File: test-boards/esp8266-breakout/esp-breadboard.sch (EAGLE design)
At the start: 6 parts

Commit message: cleanup to esp breadboard breakout
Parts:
- JP1: device esp:I2C_STANDARD -> esp:I2C_STANDARD_NO_SILK
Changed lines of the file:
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@@
 <part name="C1" library="rcl" deviceset="C-EU" device="C0805" value="1u"/>
 <part name="SUPPLY2" library="supply2" deviceset="GND" device=""/>
-<part name="JP1" library="esp" deviceset="I2C_STANDARD" device="" value="0"/>
+<part name="JP1" library="esp" deviceset="I2C_STANDARD" device="_NO_SILK" value="0"/>
 <part name="FRAME1" library="frames" deviceset="A4L-LOC" device="" value="ESP"/>
 <part name="SUPPLY3" library="supply2" deviceset="GND" device=""/>

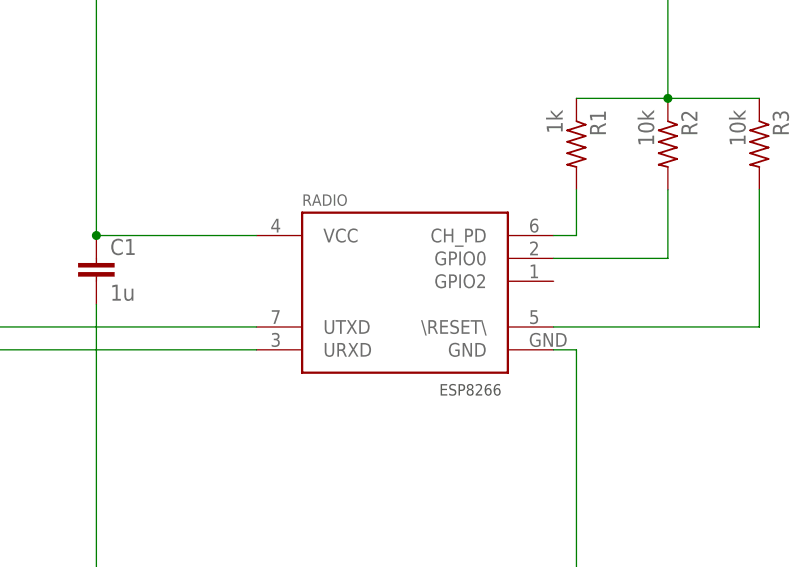
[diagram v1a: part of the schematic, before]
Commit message: ESP8266: misplaced RX and GPIO pin, switch around and resize board
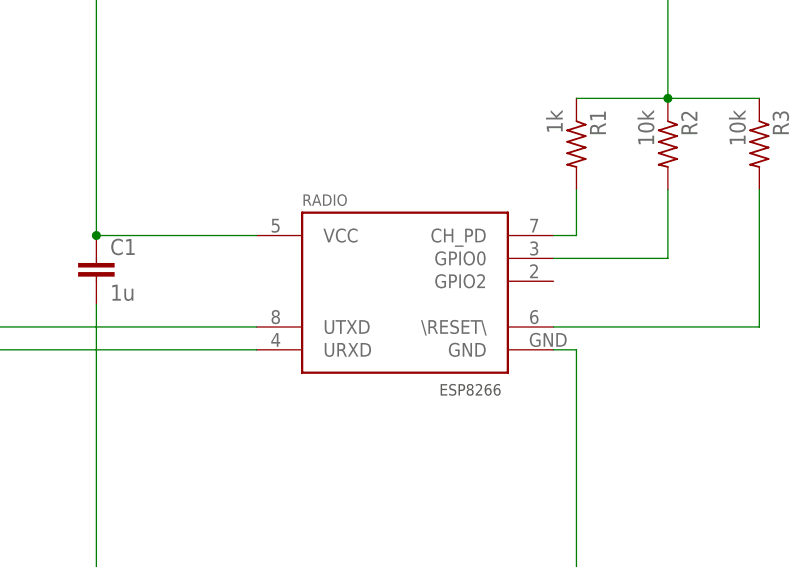
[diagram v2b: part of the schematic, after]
